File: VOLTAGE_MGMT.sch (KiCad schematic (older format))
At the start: 6 parts, among them Q1 AO3401A, U1 LMV358, U2 LP2985-3.3

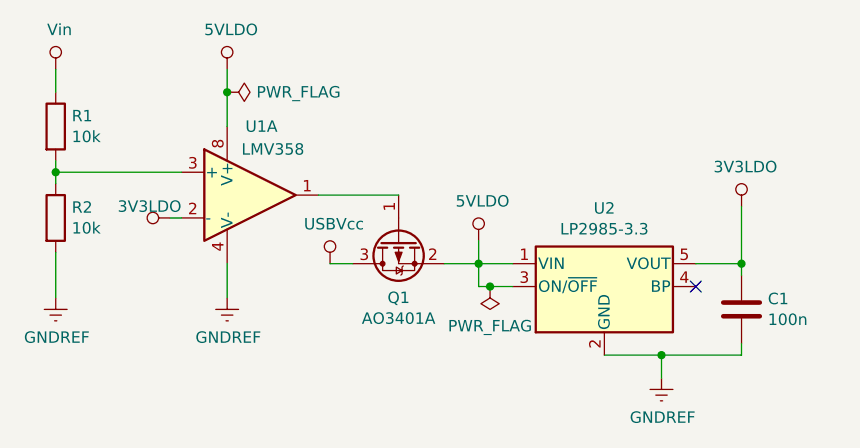
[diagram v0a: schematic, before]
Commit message: Set component footprints, added datasheets, fixed the last DRC error and a couple component values
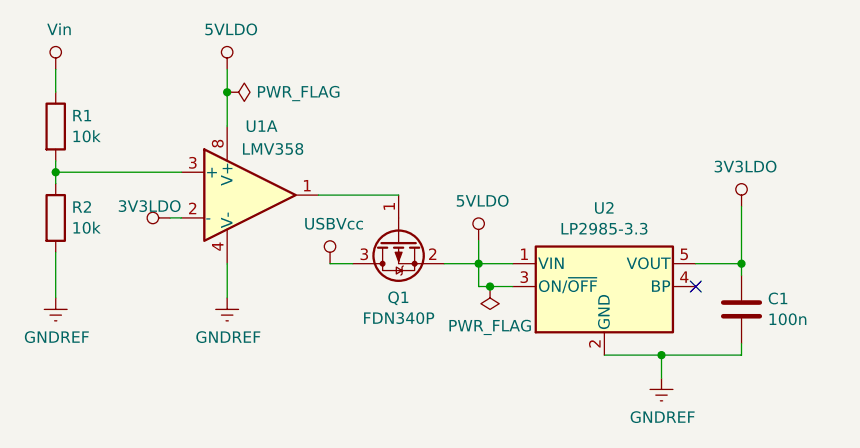
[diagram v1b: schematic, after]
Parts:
- C1: footprint (none) -> Capacitor_SMD:C_0603_1608Metric
- Q1: value AO3401A -> FDN340P
- R1, R2: footprint (none) -> Resistor_SMD:R_0603_1608Metric
- U1: footprint (none) -> Package_SO:MSOP-8_3x3mm_P0.65mm
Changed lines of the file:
@@
 F 0 "R2" H 4370 3596 50  0000 L CNN
 F 1 "10k" H 4370 3505 50  0000 L CNN
-F 2 "" V 4230 3550 50  0001 C CNN
-F 3 "~" H 4300 3550 50  0001 C CNN
+F 2 "Resistor_SMD:R_0603_1608Metric" V 4230 3550 50  0001 C CNN
+F 3 "http://www.farnell.com/datasheets/2310790.pdf" H 4300 3550 50  0001 C CNN
 	1    4300 3550
 	1    0    0    -1
@@
 F 0 "U1" H 5200 3750 50  0000 C CNN
 F 1 "LMV358" H 5250 3650 50  0000 C CNN
-F 2 "" H 5150 3450 50  0001 C CNN
-F 3 "http://www.ti.com/lit/ds/symlink/lmv324.pdf" H 5150 3450 50  0001 C CNN
+F 2 "Package_SO:MSOP-8_3x3mm_P0.65mm" H 5150 3450 50  0001 C CNN
+F 3 "http://www.farnell.com/datasheets/2140563.pdf" H 5150 3450 50  0001 C CNN
 	1    5150 3450
 	1    0    0    -1
@@
 P 5800 3650
 F 0 "Q1" V 6049 3650 50  0000 C CNN
-F 1 "AO3401A" V 6140 3650 50  0000 C CNN
+F 1 "FDN340P" V 6140 3650 50  0000 C CNN
 F 2 "Package_TO_SOT_SMD:SOT-23" H 6000 3575 50  0001 L CIN
-F 3 "http://www.aosmd.com/pdfs/datasheet/AO3401A.pdf" H 5800 3650 50  0001 L CNN
+F 3 "http://www.farnell.com/datasheets/2298381.pdf" H 5800 3650 50  0001 L CNN
 	1    5800 3650
 	0    -1   1    0
@@
 F 0 "C1" H 7415 3996 50  0000 L CNN
 F 1 "100n" H 7415 3905 50  0000 L CNN
-F 2 "" H 7338 3800 50  0001 C CNN
-F 3 "~" H 7300 3950 50  0001 C CNN
+F 2 "Capacitor_SMD:C_0603_1608Metric" H 7338 3800 50  0001 C CNN
+F 3 "http://www.farnell.com/datasheets/2739842.pdf" H 7300 3950 50  0001 C CNN
 	1    7300 3950
 	1    0    0    -1
@@
 F 0 "R1" H 4370 3196 50  0000 L CNN
 F 1 "10k" H 4370 3105 50  0000 L CNN
-F 2 "" V 4230 3150 50  0001 C CNN
-F 3 "~" H 4300 3150 50  0001 C CNN
+F 2 "Resistor_SMD:R_0603_1608Metric" V 4230 3150 50  0001 C CNN
+F 3 "http://www.farnell.com/datasheets/2310790.pdf" H 4300 3150 50  0001 C CNN
 	1    4300 3150
 	1    0    0    -1
@@
 	7100 3750 7300 3750
 $Comp
-L power:PWR_FLAG #FLG0103
+L power:PWR_FLAG #FLG02
 U 1 1 5ED979C0
 P 6200 3850
-F 0 "#FLG0103" H 6200 3925 50  0001 C CNN
+F 0 "#FLG02" H 6200 3925 50  0001 C CNN
 F 1 "PWR_FLAG" H 6200 4023 50  0000 C CNN
 F 2 "" H 6200 3850 50  0001 C CNN
@@
 	6200 3850 6300 3850
 $Comp
-L power:PWR_FLAG #FLG0104
+L power:PWR_FLAG #FLG01
 U 1 1 5ED98664
 P 5050 3000
-F 0 "#FLG0104" H 5050 3075 50  0001 C CNN
+F 0 "#FLG01" H 5050 3075 50  0001 C CNN
 F 1 "PWR_FLAG" V 5050 3128 50  0000 L CNN
 F 2 "" H 5050 3000 50  0001 C CNN

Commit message: Updated the schematic, added missing footprints, started PCB design
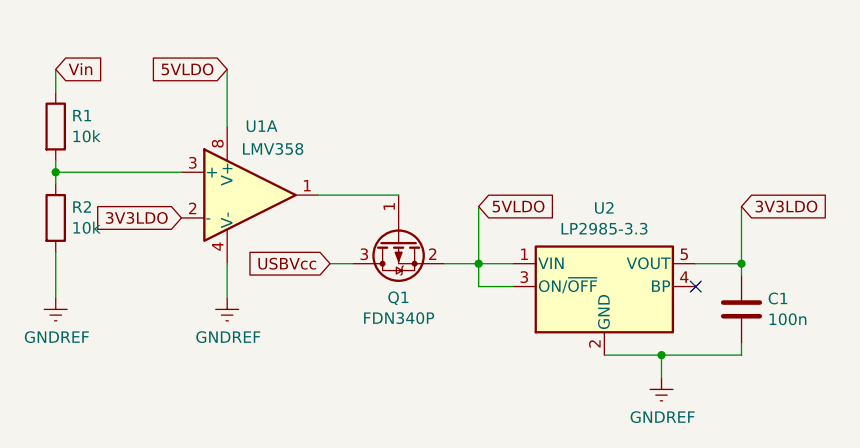
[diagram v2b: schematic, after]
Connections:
- net Vin: now reaches R1.1
- net 3V3LDO: now reaches U1.2 (-)
- net 3V3LDO: now also C1.1, U2.5 (VOUT)
- net 5VLDO: now reaches U1.8 (V+)
- net 5VLDO: now also Q1.2 (S), U2.1 (VIN), U2.3 (ON/~OFF~)
- net USBVcc: now reaches Q1.3 (D)
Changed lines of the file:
@@
 Wire Wire Line
 	4300 3300 4300 3350
-$Comp
-L power_symbols:Vin #PWR01
-U 1 1 5EC75D75
-P 4300 2900
-F 0 "#PWR01" H 4300 2750 50  0001 C CNN
-F 1 "Vin" H 4317 3073 50  0000 C CNN
-F 2 "" H 4300 2900 50  0001 C CNN
-F 3 "" H 4300 2900 50  0001 C CNN
-	1    4300 2900
-	1    0    0    -1
-$EndComp
 Wire Wire Line
 	4300 2900 4300 3000
@@
 Wire Wire Line
 	4300 3350 4850 3350
-Wire Wire Line
-	4850 3550 4800 3550
-$Comp
-L power_symbols:3V3LDO #PWR04
-U 1 1 5EC75D86
-P 4800 3550
-F 0 "#PWR04" H 4800 3400 50  0001 C CNN
-F 1 "3V3LDO" V 4850 3500 50  0000 L CNN
-F 2 "" H 4800 3550 50  0001 C CNN
-F 3 "" H 4800 3550 50  0001 C CNN
-	1    4800 3550
-	0    -1   -1   0
-$EndComp
 $Comp
 L power:GNDREF #PWR07
@@
 	5050 3900 5050 3750
 $Comp
-L power_symbols:5VLDO #PWR02
-U 1 1 5EC75DA0
-P 5050 2900
-F 0 "#PWR02" H 5050 2750 50  0001 C CNN
-F 1 "5VLDO" H 5067 3073 50  0000 C CNN
-F 2 "" H 5050 2900 50  0001 C CNN
-F 3 "" H 5050 2900 50  0001 C CNN
-	1    5050 2900
-	1    0    0    -1
-$EndComp
-Wire Wire Line
-	5050 2900 5050 3000
-$Comp
 L Transistor_FET:AO3401A Q1
 U 1 1 5EC75DA7
@@
 	0    -1   1    0
 $EndComp
-$Comp
-L power_symbols:USBVcc #PWR06
-U 1 1 5EC75DAD
-P 5500 3750
-F 0 "#PWR06" H 5500 3600 50  0001 C CNN
-F 1 "USBVcc" H 5517 3923 50  0000 C CNN
-F 2 "" H 5500 3750 50  0001 C CNN
-F 3 "" H 5500 3750 50  0001 C CNN
-	1    5500 3750
-	1    0    0    -1
-$EndComp
 Wire Wire Line
 	5500 3750 5600 3750
-$Comp
-L power_symbols:5VLDO #PWR05
-U 1 1 5EC75DB4
-P 6150 3650
-F 0 "#PWR05" H 6150 3500 50  0001 C CNN
-F 1 "5VLDO" H 6167 3823 50  0000 C CNN
-F 2 "" H 6150 3650 50  0001 C CNN
-F 3 "" H 6150 3650 50  0001 C CNN
-	1    6150 3650
-	1    0    0    -1
-$EndComp
 Wire Wire Line
 	6000 3750 6150 3750
 Wire Wire Line
-	6150 3750 6150 3650
+	6150 3750 6150 3500
 $Comp
 L Regulator_Linear:LP2985-3.3 U2
@@
 Wire Wire Line
 	7300 3800 7300 3750
-$Comp
-L power_symbols:3V3LDO #PWR03
-U 1 1 5EC75DD8
-P 7300 3500
-F 0 "#PWR03" H 7300 3350 50  0001 C CNN
-F 1 "3V3LDO" H 7317 3673 50  0000 C CNN
-F 2 "" H 7300 3500 50  0001 C CNN
-F 3 "" H 7300 3500 50  0001 C CNN
-	1    7300 3500
-	1    0    0    -1
-$EndComp
 Wire Wire Line
 	7300 3500 7300 3750
@@
 Wire Wire Line
 	6150 3850 6150 3750
-Wire Wire Line
-	6150 3850 6200 3850
 $Comp
 L Device:R R1
@@
 Wire Wire Line
 	7100 3750 7300 3750
-$Comp
-L power:PWR_FLAG #FLG02
-U 1 1 5ED979C0
-P 6200 3850
-F 0 "#FLG02" H 6200 3925 50  0001 C CNN
-F 1 "PWR_FLAG" H 6200 4023 50  0000 C CNN
-F 2 "" H 6200 3850 50  0001 C CNN
-F 3 "~" H 6200 3850 50  0001 C CNN
-	1    6200 3850
-	-1   0    0    1
-$EndComp
-Connection ~ 6200 3850
+Text GLabel 4300 2900 2    50   Input ~ 0
+Vin
+Text GLabel 5050 2900 0    50   Input ~ 0
+5VLDO
+Text GLabel 7300 3500 2    50   Input ~ 0
+3V3LDO
+Text GLabel 4850 3550 0    50   Input ~ 0
+3V3LDO
+Text GLabel 5500 3750 0    50   Input ~ 0
+USBVcc
+Text GLabel 6150 3500 2    50   Input ~ 0
+5VLDO
 Wire Wire Line
-	6200 3850 6300 3850
-$Comp
-L power:PWR_FLAG #FLG01
-U 1 1 5ED98664
-P 5050 3000
-F 0 "#FLG01" H 5050 3075 50  0001 C CNN
-F 1 "PWR_FLAG" V 5050 3128 50  0000 L CNN
-F 2 "" H 5050 3000 50  0001 C CNN
-F 3 "~" H 5050 3000 50  0001 C CNN
-	1    5050 3000
-	0    1    1    0
-$EndComp
-Connection ~ 5050 3000
+	5050 2900 5050 3150
 Wire Wire Line
-	5050 3000 5050 3150
+	6150 3850 6300 3850
 $EndSCHEMATC
